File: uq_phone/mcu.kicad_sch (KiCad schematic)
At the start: 21 parts, among them J6 Conn_ARM_SWD_TagConnect_TC2030, U5 TXB0108RGYR, U6 TXB0108RGYR, U7 STM32H730VBTx

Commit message: Update Keypad
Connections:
- net PB_HASH: now reaches U7.1 (PE2)
- net PB_8: now reaches U7.12 (PH0)
- net PB_9: now reaches U7.13 (PH1)
- net PB_MENU_L: now reaches U7.15 (PC0)
- net PB_MENU_R: now reaches U7.16 (PC1)
- net PB_1: now reaches U7.2 (PE3)
- net PB_PWR: now reaches U7.22 (PA0)
- net PB_VOL_DOWN: now reaches U7.23 (PA1)
- net PB_VOL_UP: now reaches U7.24 (PA2)
- net LED_DATA: now reaches U7.25 (PA3)
- net PB_2: now reaches U7.3 (PE4)
- net PB_3: now reaches U7.4 (PE5)
- net PB_4: now reaches U7.5 (PE6)
- net PB_5: now reaches U7.7 (PC13)
- net PB_END_CALL: now reaches U7.77 (PA15(JTDI))
- net PB_6: now reaches U7.8 (PC14)
- net PB_CALL: now reaches U7.87 (PD6)
- net PB_DPAD_UP: now reaches U7.89 (PB3(JTDO)
- net PB_7: now reaches U7.9 (PC15)
- net PB_DPAD_DOWN: now reaches U7.90 (PB4(NJTRST))
- net PB_DPAD_RIGHT: now reaches U7.91 (PB5)
- net PB_DPAD_LEFT: now reaches U7.92 (PB6)
- net PB_DPAD_SELECT: now reaches U7.93 (PB7)
- net PB_STAR: now reaches U7.97 (PE0)
- net PB_0: now reaches U7.98 (PE1)
- no-connect marks 4 -> 6

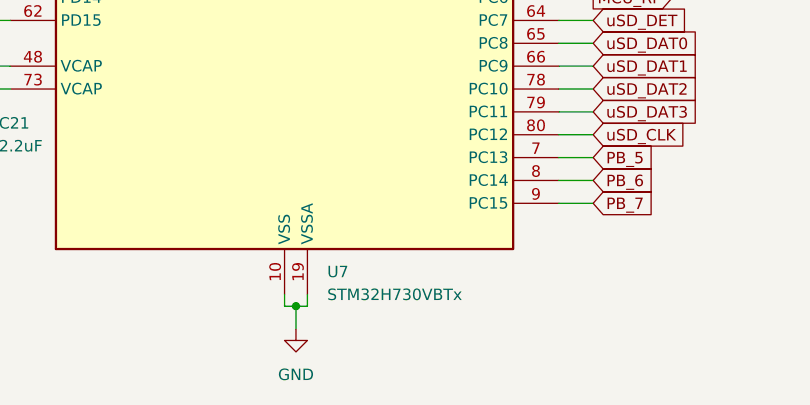
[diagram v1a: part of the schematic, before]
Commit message: Change MCU to h733VG
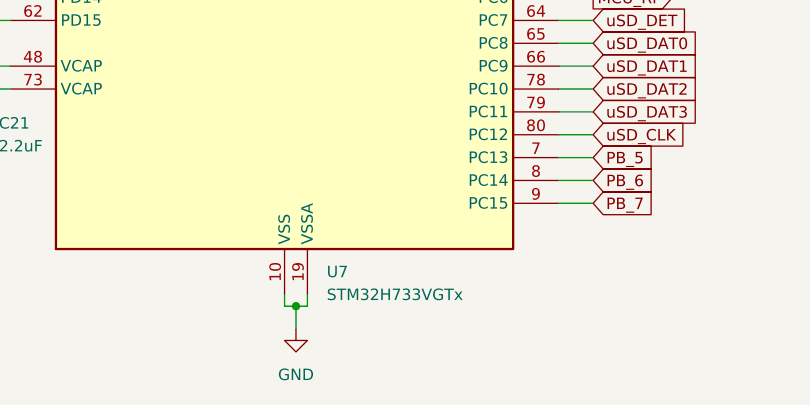
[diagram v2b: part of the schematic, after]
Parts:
- removed U7: STM32H730VBTx, Package_QFP:LQFP-100_14x14mm_P0.5mm, symbol MCU_ST_STM32H7:STM32H730VBTx
- added U7: STM32H733VGTx, Package_QFP:LQFP-100_14x14mm_P0.5mm, symbol MCU_ST_STM32H7:STM32H733VGTx
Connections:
- net +3.3V: now also U7.100 (VDD), U7.11 (VDD), U7.27 (VDD), U7.50 (VDD), U7.75 (VDD)
- net AUD_SW_H: now also U7.34 (PB0)
- net DISP_BL: now also U7.46 (PB10)
- net DISP_CS: now also U7.88 (PD7)
- net DISP_DB0: now also U7.61 (PD14)
- net DISP_DB1: now also U7.62 (PD15)
- net DISP_DB10: now also U7.43 (PE13)
- net DISP_DB11: now also U7.44 (PE14)
- net DISP_DB12: now also U7.45 (PE15)
- net DISP_DB13: now also U7.55 (PD8)
- net DISP_DB14: now also U7.56 (PD9)
- net DISP_DB15: now also U7.57 (PD10)
- net DISP_DB2: now also U7.81 (PD0)
- net DISP_DB3: now also U7.82 (PD1)
- net DISP_DB4: now also U7.37 (PE7)
- net DISP_DB5: now also U7.38 (PE8)
- net DISP_DB6: now also U7.39 (PE9)
- net DISP_DB7: now also U7.40 (PE10)
- net DISP_DB8: now also U7.41 (PE11)
- net DISP_DB9: now also U7.42 (PE12)
- net DISP_DC: now also U7.58 (PD11)
- net DISP_RD: now also U7.85 (PD4)
- net DISP_RES: now also U7.84 (PD3)
- net DISP_WR: now also U7.86 (PD5)
- net FUEL_GPO: now also U7.51 (PB12)
- net GND: now also U7.10 (VSS), U7.19 (VSSA), U7.26 (VSS), U7.49 (VSS), U7.74 (VSS), U7.94 (BOOT0), U7.99 (VSS)
- net HP_DET_MCU: now also U7.33 (PC5)
- net LED_DATA: now also U7.25 (PA3)
- net MCP_PG: now also U7.52 (PB13)
- net MCP_STAT1: now also U7.54 (PB15)
- net MCP_STAT2: now also U7.53 (PB14)
- net MCU_AUD_BCLK_H: now also U7.29 (PA5)
- net MCU_AUD_OUT_L_H: now also U7.31 (PA7)
- net MCU_AUD_SYNC_H: now also U7.28 (PA4)
- net MCU_CTS: now also U7.70 (PA11)
- net MCU_DCD: now also U7.59 (PD12)
- net MCU_DSR: now also U7.67 (PA8)
- net MCU_DTR: now also U7.60 (PD13)
- net MCU_RI: now also U7.63 (PC6)
- net MCU_RTS: now also U7.71 (PA12)
- net MCU_RXD: now also U7.68 (PA9)
- net MCU_TXD: now also U7.69 (PA10)
- net MOB_PWR_CTL: now also U7.36 (PB2)
- net MOB_RST_CTL: now also U7.47 (PB11)
- net MOB_WAKE_H: now also U7.35 (PB1)
- net PB_0: now also U7.98 (PE1)
- net PB_1: now also U7.2 (PE3)
- net PB_2: now also U7.3 (PE4)
- net PB_3: now also U7.4 (PE5)
- net PB_4: now also U7.5 (PE6)
- net PB_5: now also U7.7 (PC13)
- net PB_6: now also U7.8 (PC14)
- net PB_7: now also U7.9 (PC15)
- net PB_8: now also U7.12 (PH0)
- net PB_9: now also U7.13 (PH1)
- net PB_CALL: now also U7.87 (PD6)
- net PB_DPAD_DOWN: now also U7.90 (PB4(NJTRST))
- net PB_DPAD_LEFT: now also U7.92 (PB6)
- net PB_DPAD_RIGHT: now also U7.91 (PB5)
- net PB_DPAD_SELECT: now also U7.93 (PB7)
- net PB_DPAD_UP: now also U7.89 (PB3(JTDO)
- net PB_END_CALL: now also U7.77 (PA15(JTDI))
- net PB_HASH: now also U7.1 (PE2)
- net PB_MENU_L: now also U7.15 (PC0)
- net PB_MENU_R: now also U7.16 (PC1)
- net PB_PWR: now also U7.22 (PA0)
- net PB_STAR: now also U7.97 (PE0)
- net PB_VOL_DOWN: now also U7.23 (PA1)
- net PB_VOL_UP: now also U7.24 (PA2)
- net RST: now also U7.14 (NRST)
- net SCL: now also U7.95 (PB8)
- net SDA: now also U7.96 (PB9)
- net SWCLK: now also U7.76 (PA14(JTCK)
- net SWDIO: now also U7.72 (PA13(JTMS)
- net VIB_EN: now also U7.32 (PC4)
- net VIB_PWM: now also U7.30 (PA6)
- net uSD_CLK: now also U7.80 (PC12)
- net uSD_CMD: now also U7.83 (PD2)
- net uSD_DAT0: now also U7.65 (PC8)
- net uSD_DAT1: now also U7.66 (PC9)
- net uSD_DAT2: now also U7.78 (PC10)
- net uSD_DAT3: now also U7.79 (PC11)
- net uSD_DET: now also U7.64 (PC7)
- net at C21.1: now also U7.73 (VCAP)
- net at C20.1: now also U7.48 (VCAP)

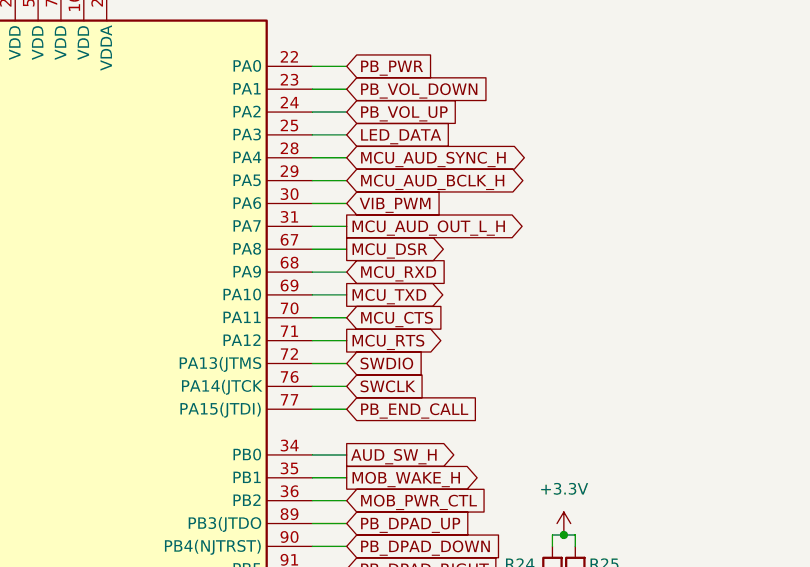
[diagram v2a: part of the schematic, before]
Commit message: Swap RX TX
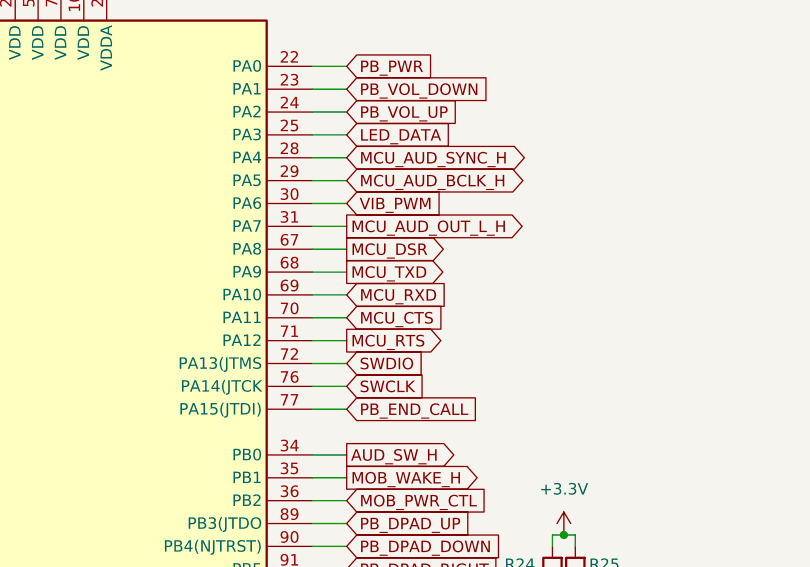
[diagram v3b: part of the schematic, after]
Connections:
- net MCU_RXD: now also U7.69 (PA10); no longer U7.68 (PA9)
- net MCU_TXD: now also U7.68 (PA9); no longer U7.69 (PA10)

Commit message: Update Various Connectors
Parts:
- removed R24, R25: 10k, Resistor_SMD:R_0402_1005Metric, symbol Resistors:Resistor_10k
- added R24, R25: 4.7k, Resistor_SMD:R_0402_1005Metric, symbol Resistors:Resistor_4k7
- added R49: 10k, Resistor_SMD:R_0402_1005Metric, symbol Resistors:Resistor_10k
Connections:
- net +3.3V: now also R24.2, R25.2
- net GND: now also R49.1; no longer U7.94 (BOOT0)
- net SCL: now also R24.1
- net SDA: now also R25.1
- new net: R49.2, U7.94 (BOOT0)
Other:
- note added: "ENSURE VREF"
- note added: "make pullup 4.7k"
- moved on the sheet: C18

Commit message: Generate Early production outputs
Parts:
- C14, C15, C16, C17, C18, C22, C23, C24, C25, C26: LCSC PN (none) -> C307331
- C19: LCSC PN (none) -> C191541
- C20, C21: LCSC PN (none) -> C107369
- R24, R25: LCSC PN (none) -> C606173
- R26, R27, R49: LCSC PN (none) -> C851848
- U5, U6: LCSC PN (none) -> C194701
